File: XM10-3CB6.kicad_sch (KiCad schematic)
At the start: 1 part, among them U1 EL84

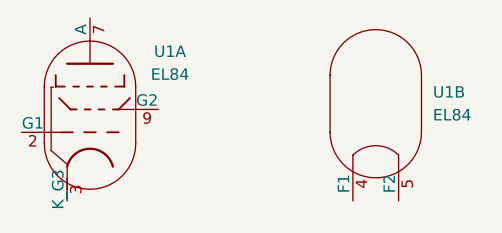
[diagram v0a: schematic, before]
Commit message: Fix 3CB6 pin mapping
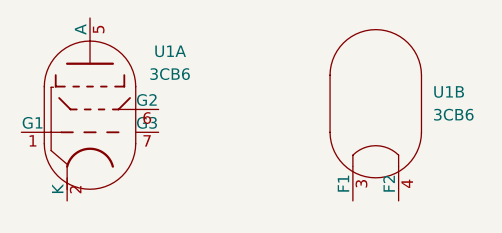
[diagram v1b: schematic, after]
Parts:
- U1: value EL84 -> 3CB6; footprint Valve:Valve_Noval_P -> Valve:Valve_B7G_P; symbol Valve:EL84 -> Valve:3CB6
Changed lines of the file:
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@@
 	(paper "A4")
 	(symbol
-		(lib_id "Valve:EL84")
+(lib_id "Valve:3CB6")
 		(at 151.13 87.63 0)
 		(unit 2)
@@
 			)
 		)
-		(property "Value" "EL84"
+(property "Value" "3CB6"
 			(at 157.48 88.2649 0)
 			(effects
@@
 			)
 		)
-		(property "Footprint" "Valve:Valve_Noval_P"
+(property "Footprint" "Valve:Valve_B7G_P"
 			(at 158.75 97.79 0)
 			(effects
@@
 			)
 		)
-		(property "Datasheet" "http://www.r-type.org/pdfs/el84.pdf"
+(property "Datasheet" "http://www.r-type.org/pdfs/3cb6.pdf"
 			(at 151.13 87.63 0)
 			(effects
@@
 			)
 		)
-		(pin "7"
-		)
-		(pin "3"
-		)
-		(pin "2"
-		)
-		(pin "4"
-		)
-		(pin "9"
-		)
-		(pin "5"
-		)
+                (pin "5"
+                )
+                (pin "2"
+                )
+                (pin "1"
+                )
+                (pin "3"
+                )
+                (pin "6"
+                )
+                (pin "4"
+                )
+                (pin "7"
+                )
 		(instances
 			(project ""
@@
 	)
 	(symbol
-		(lib_id "Valve:EL84")
+(lib_id "Valve:3CB6")
 		(at 119.38 88.9 0)
 		(unit 1)
@@
 			)
 		)
-		(property "Value" "EL84"
+(property "Value" "3CB6"
 			(at 128.27 83.7498 0)
 			(effects
@@
 			)
 		)
-		(property "Footprint" "Valve:Valve_Noval_P"
+(property "Footprint" "Valve:Valve_B7G_P"
 			(at 127 99.06 0)
 			(effects
@@
 			)
 		)
-		(property "Datasheet" "http://www.r-type.org/pdfs/el84.pdf"
+(property "Datasheet" "http://www.r-type.org/pdfs/3cb6.pdf"
 			(at 119.38 88.9 0)
 			(effects
@@
 			)
 		)
-		(pin "7"
-		)
-		(pin "3"
-		)
-		(pin "2"
-		)
-		(pin "4"
-		)
-		(pin "9"
-		)
-		(pin "5"
-		)
+                (pin "5"
+                )
+                (pin "2"
+                )
+                (pin "1"
+                )
+                (pin "3"
+                )
+                (pin "6"
+                )
+                (pin "4"
+                )
+                (pin "7"
+                )
 		(instances
 			(project ""
